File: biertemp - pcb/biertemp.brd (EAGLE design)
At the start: 100 x 80 mm, 32 parts, among them IC1 MEGA8-P, K1 G5LE, Q1 12MHz, Q2 32,768kHz

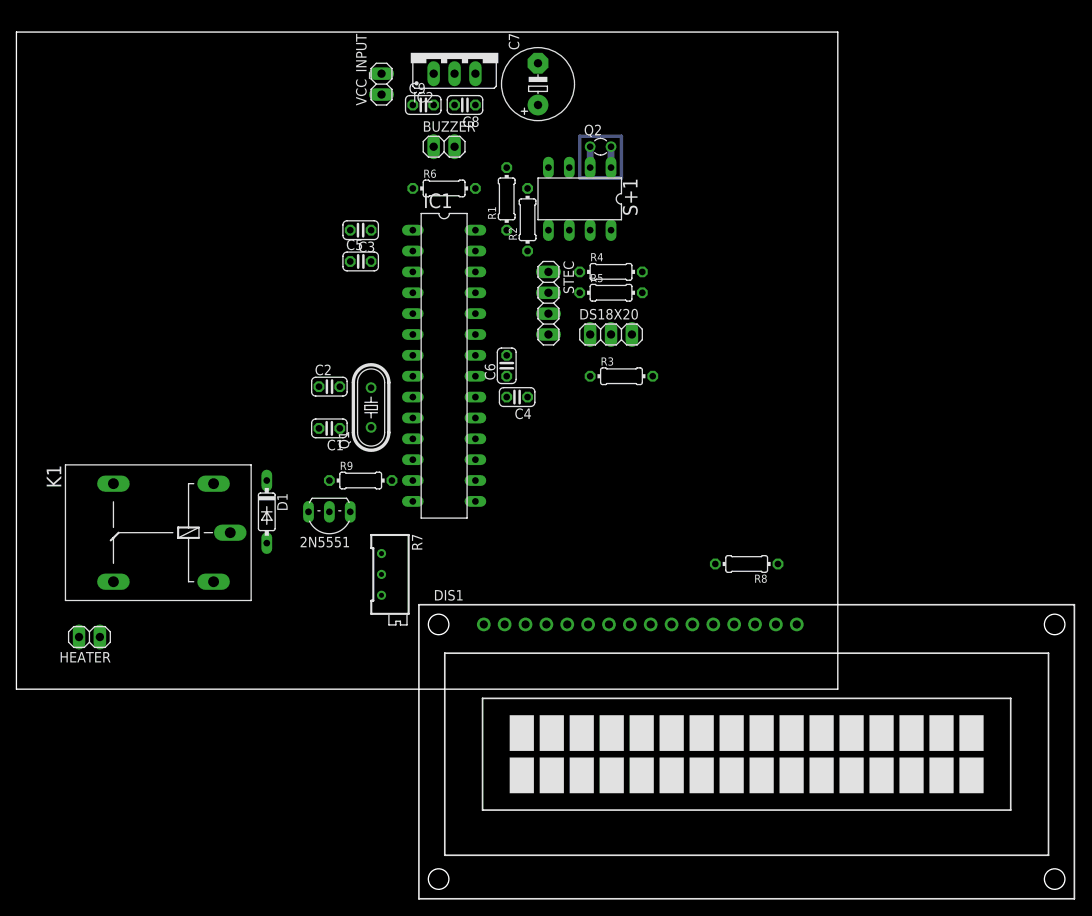
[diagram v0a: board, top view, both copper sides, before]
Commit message: first pcb version finished, including pcb design changed ports for better layout NEW: All port definitions now with macros
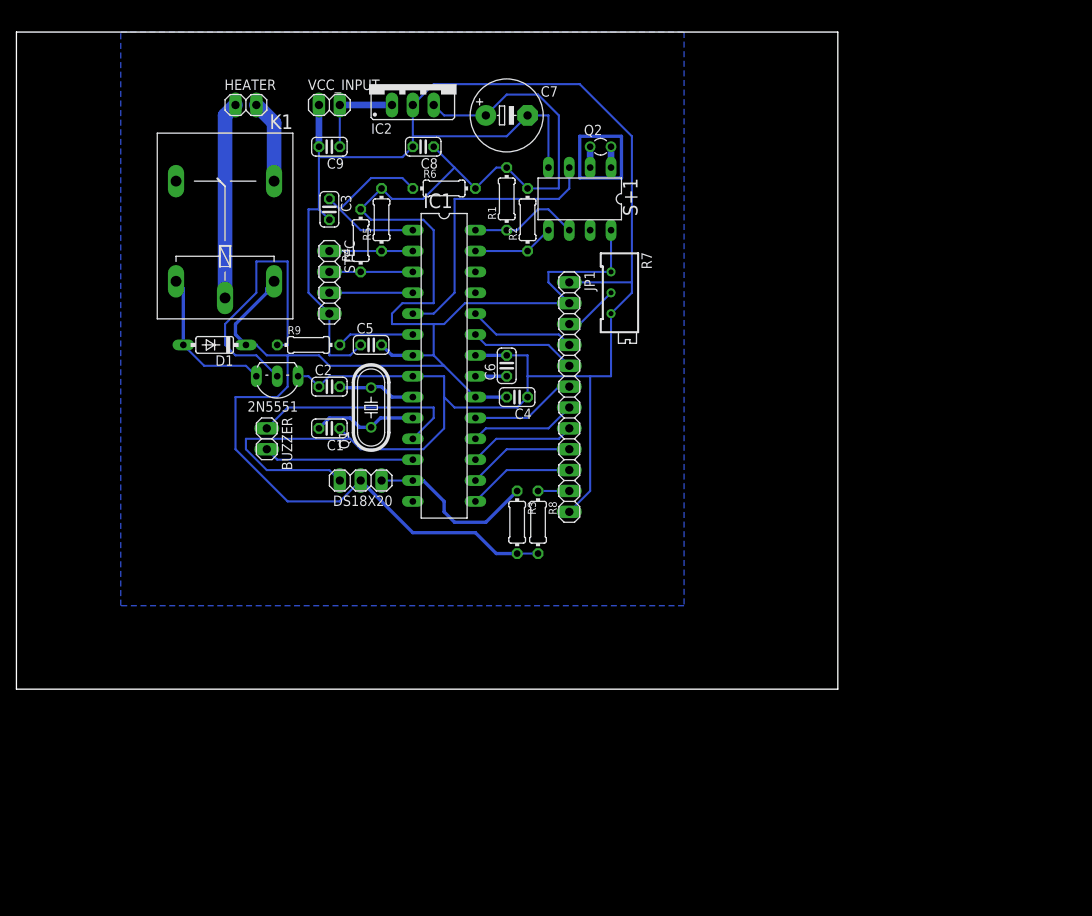
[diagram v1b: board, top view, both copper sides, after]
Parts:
- removed DIS1: TUXGR_16X2_R2, display-lcd:TUXGR_16X2_R2
- added JP1: (no value), pinhead:1X12
- R1: value (none) -> 4,7
- R2, R3: value (none) -> 4,7k
- R4, R5: value (none) -> 10k
- moved HEATER 67.5 mm to (27.9, 71.1), turned to 0 degrees
- moved R7 44.2 mm to (73.7, 48.3)
- moved BUZZER 41.6 mm to (30.5, 30.5), turned to 270 degrees
- moved K1 39.1 mm to (25.4, 57.1), turned to 90 degrees
- moved DS18X20 35.3 mm to (41.9, 25.4), turned to 180 degrees
- moved R4 30.7 mm to (41.9, 54.6), turned to 90 degrees
- moved R5 29.3 mm to (44.5, 57.1), turned to 90 degrees
- moved STEC 26.8 mm to (38.1, 49.5)
- moved R8 25.9 mm to (63.5, 20.3), turned to 270 degrees
- moved R3 21.8 mm to (61.0, 20.3), turned to 270 degrees
- moved D1 21.3 mm to (24.1, 41.9), turned to 180 degrees
- moved 2N5551 17.7 mm to (31.8, 36.8)
- moved R9 17.7 mm to (35.6, 41.9)
- moved C9 12.5 mm to (38.1, 66.0), turned to 180 degrees
- moved C5 10.2 mm to (43.2, 41.9)
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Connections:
- net +5V: now also JP1.2; no longer DIS1.2
- net GND: now also JP1.1, JP1.12; no longer DIS1.1, DIS1.16
- net N$14: now also IC1.15, JP1.10; no longer DIS1.14, IC1.14
- net N$15: now also JP1.11; no longer DIS1.15
- net N$16: now also JP1.3; no longer DIS1.3
- net N$17: now also IC1.16, JP1.9; no longer DIS1.4, IC1.18
- net N$18: now also IC1.17, JP1.8; no longer DIS1.5, IC1.19
- net N$19: now also IC1.18, JP1.7; no longer DIS1.6, IC1.23
- net N$2: now also IC1.13; no longer IC1.24
- net N$20: now also IC1.19, JP1.6; no longer DIS1.11, IC1.17
- net N$21: now also IC1.23, JP1.5; no longer DIS1.12, IC1.16
- net N$22: now also IC1.24, JP1.4; no longer DIS1.13, IC1.15
- net N$24: now also IC1.11; no longer IC1.2
- net N$25: now also IC1.2, R5.1, STEC.1; no longer BUZZER.2, IC1.3
- net N$26: now also BUZZER.2, IC1.12; no longer IC1.13, R9.2
- net N$8: now also IC1.6, R9.2; no longer IC1.25, R4.1, STEC.1
- net N$9: now also IC1.3, R4.1; no longer IC1.26, R5.1
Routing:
- net GND: track 0.00 -> 265.4 mm
- net +5V: track 0.00 -> 245.0 mm
- net N$27: track 0.00 -> 34.9 mm
- net N$11: track 0.00 -> 34.6 mm
- net N$24: track 0.00 -> 26.2 mm
- net N$31: track 0.00 -> 24.0 mm
- net N$5: track 0.00 -> 22.7 mm
- net N$2: track 0.00 -> 20.9 mm
- net N$28: track 0.00 -> 18.6 mm
- net N$26: track 0.00 -> 18.3 mm
- net N$13: track 0.00 -> 13.5 mm
- net N$22: track 0.00 -> 13.0 mm
- net N$17: track 0.00 -> 13.0 mm
- net N$14: track 0.00 -> 13.0 mm
- net N$21: track 0.00 -> 13.0 mm
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- added copper zone on layer 16, net GND

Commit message: UPDATE: changed PCB Layout
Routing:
- net N$23: track 20.3 -> 0.00 mm
- net +5V: track 245.0 -> 240.5 mm
- net N$27: track 34.9 -> 38.8 mm
- net N$11: track 34.6 -> 33.9 mm

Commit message: PCB Update
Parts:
- removed HEATER: (no value), pinhead:1X02
- added HEATER1, HEATER2: (no value), pinhead:1X01
- moved BUZZER 1.27 mm to (31.8, 30.5)
- moved C1 0.63 mm to (38.7, 31.8), turned to 90 degrees
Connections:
- net N$31: now also HEATER1.1; no longer HEATER.1
- net N$32: now also HEATER2.1; no longer HEATER.2
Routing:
- net GND: track 265.4 -> 242.7 mm
- net +5V: track 240.5 -> 244.7 mm
- net N$27: track 38.8 -> 36.1 mm
- net N$7: track 12.9 -> 11.1 mm
- net N$24: track 26.2 -> 24.6 mm
- net N$31: track 24.0 -> 25.4 mm
- net N$26: track 18.3 -> 17.0 mm
- net N$21: track 13.0 -> 14.3 mm
- net N$32: track 10.2 -> 11.3 mm
